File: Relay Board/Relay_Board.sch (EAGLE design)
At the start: 45 parts, among them J1 22-05-7048-04, J2 22-05-7028-02, J3 22-05-7028-02, K1 G6K-2G-Y, K2 G6K-2G-Y, K3 G6K-2G-Y, K4 G6K-2G-Y, T1 EXMACHINA-LOGO-NAME, U10 SN74LVC2G17DBVR, U9 SN74LVC2G17DBVR, X1 MSTBA2, X12 22-05-7028-02, X13 22-05-7028-02, X14 22-05-7038-03, X15 22-05-7038-03

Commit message: Add free-wheel diode on the schematic and re-route the board
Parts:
- added D1, D2, D3, D4: STPS3L40UF, diode:STPS3L40UF
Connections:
- net GND: now also D1.A, D2.A, D3.A, D4.A
- net N$24: now also D1.C
- net N$28: now also D3.C
- net N$33: now also D4.C
- net N$55: now also D2.C
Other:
- moved on the sheet: C129, C130, C131, C132, C133, C134, J2-1, J2-2, J3-1, J3-2, K1, K2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

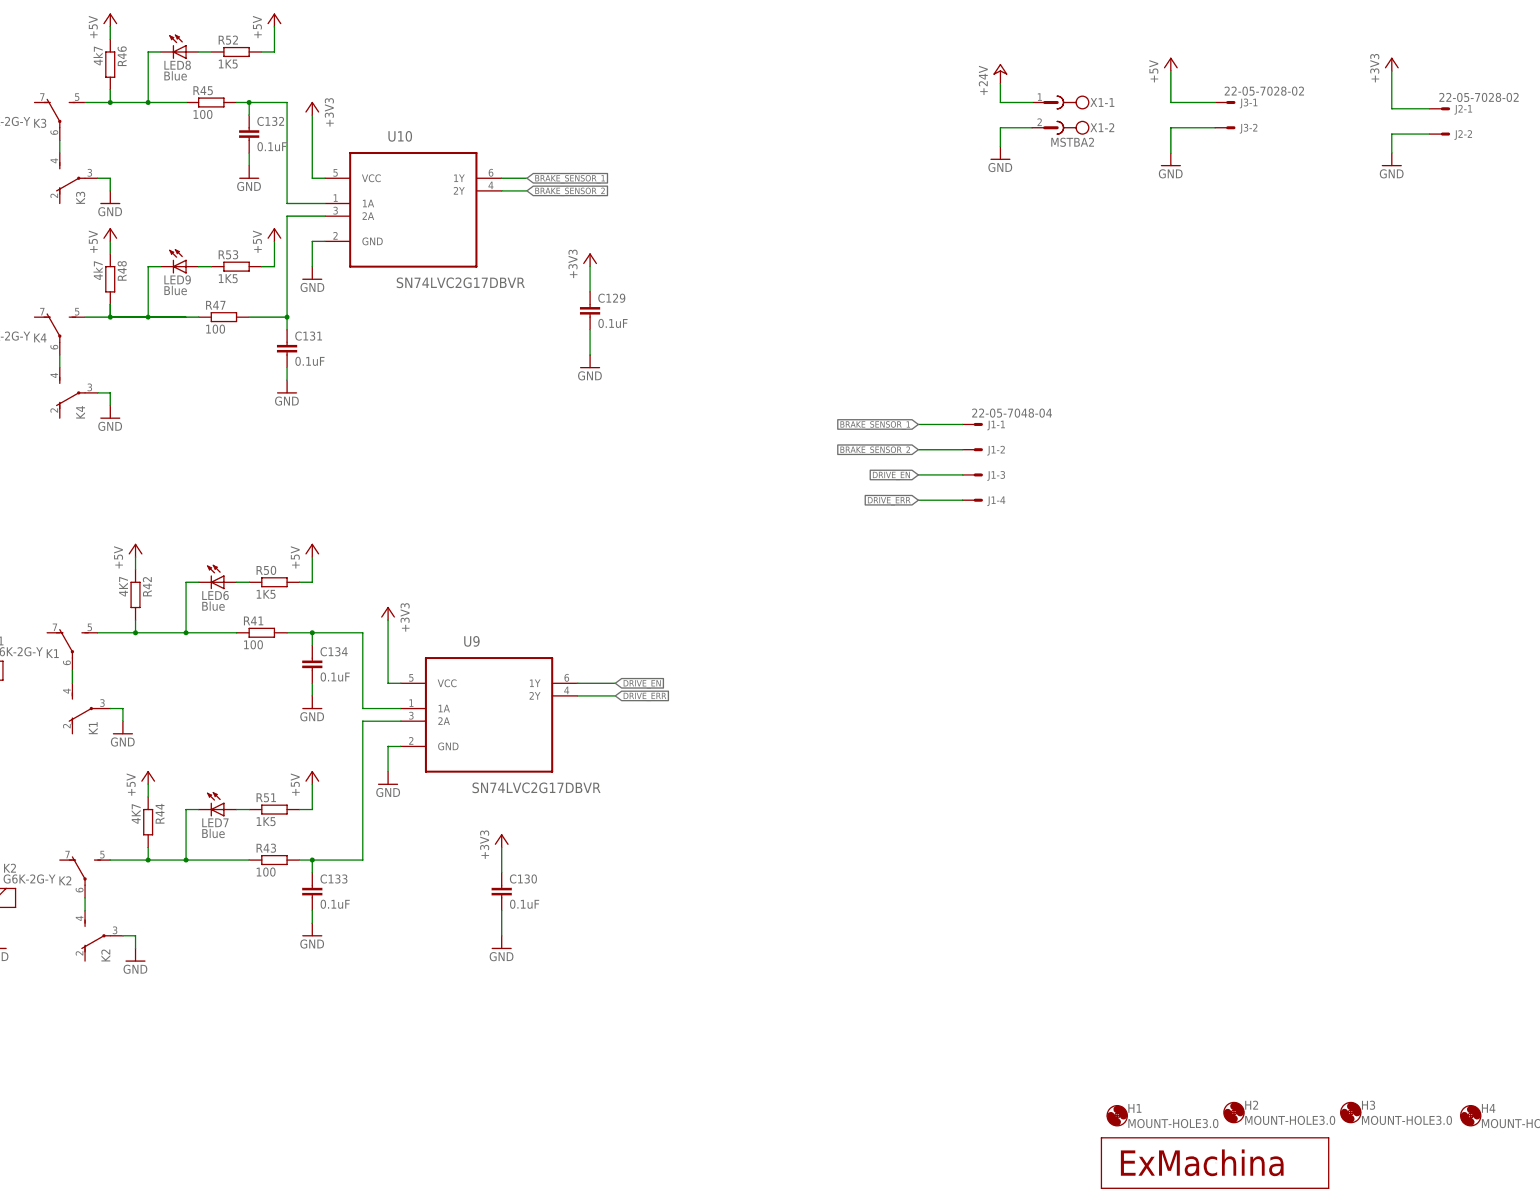
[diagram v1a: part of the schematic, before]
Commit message: Add fiducial to the board
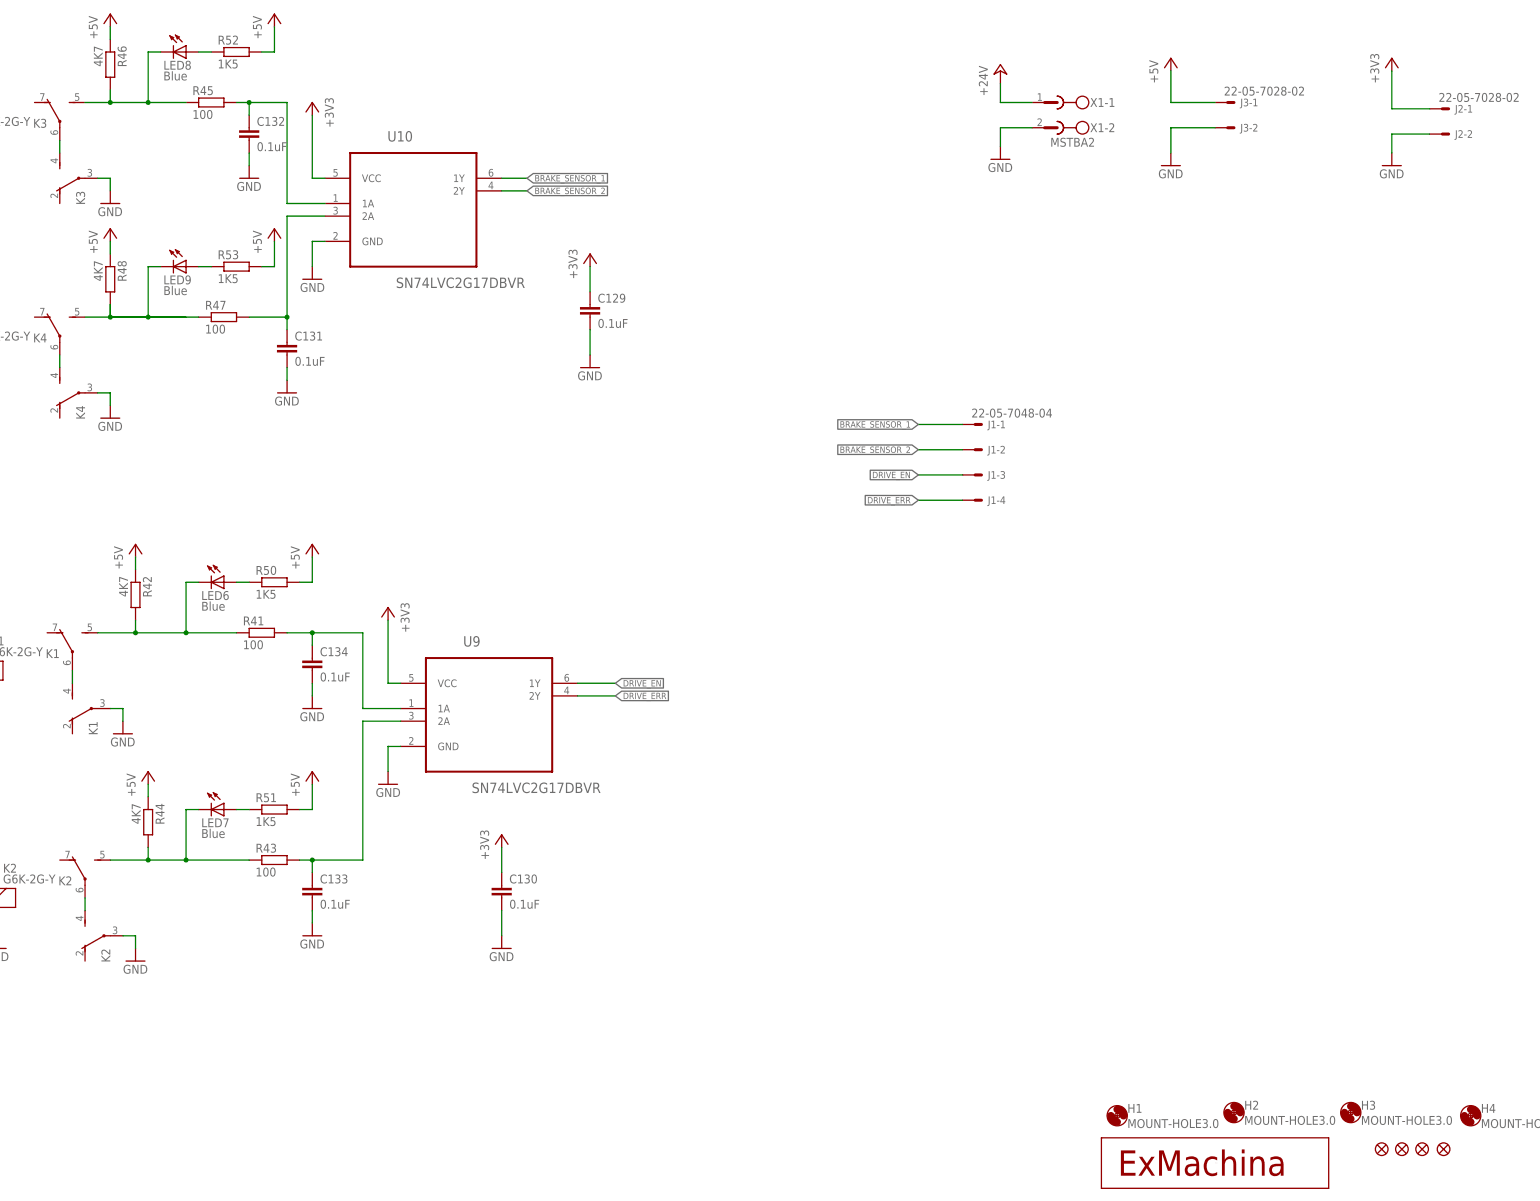
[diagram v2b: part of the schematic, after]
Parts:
- added JP1, JP2, JP3, JP4: FIDUCIAL1X2, SparkFun:FIDUCIAL1X2
- C129, C130, C131, C132, C133, C134: MPN (none) -> MC0603B104K250CT; OC_NEWARK (none) -> 06R4925
- D1, D2, D3, D4: OC_NEWARK (none) -> 06X0873
- H1, H2, H3, H4, T1: OC_NEWARK (none) -> unknown
- J1: MPN (none) -> 22-05-7048; OC_NEWARK (none) -> 26M6363
- J2, J3, X12, X13: MPN (none) -> 22-05-7028; OC_NEWARK (none) -> 25M1728
- K1, K2, K3, K4: MPN (none) -> G6K-2G-Y 24DC; OC_NEWARK (none) -> 82T9378
- LED6, LED7, LED8, LED9: MPN (none) -> OVS-0603; OC_NEWARK (none) -> 15R2205
- R108, R109, R110, R111, R41, R43, R45, R47: MPN (none) -> MCMR06X1000FTL; OC_NEWARK (none) -> 86T3504
- R42, R44: MPN (none) -> MCMR06X4701FTL; OC_NEWARK (none) -> 86T3649
- R46, R48: value 4k7 -> 4K7; MPN (none) -> MCMR06X4701FTL; OC_NEWARK (none) -> 86T3649
- R50, R51, R52, R53: MPN (none) -> MCMR06X1501FTL; OC_NEWARK (none) -> 86T3542
- U10, U9: MF (none) -> TEXAS INSTRUMENTS
- X14, X15: MPN (none) -> 22-05-7038; OC_NEWARK (none) -> 26M6362

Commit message: Change name and value size on the board
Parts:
- removed X12: 22-05-7028-02, con-molex:22-05-7028-02
- removed X14, X15: 22-05-7038-03, con-molex:22-05-7038-03
- added J5: 22-05-7048-04, con-molex:22-05-7048-04
- added J6, J7: 22-05-7028-02, con-molex:22-05-7028-02
- J1: value 22-05-7048-04 -> 22-05-7038-03; device con-molex:22-05-7048-04 -> con-molex:22-05-7038-03; MPN 22-05-7048 -> 22-05-7038; OC_NEWARK 26M6363 -> 26M6362
- J2: value 22-05-7028-02 -> 22-05-7038-03; device con-molex:22-05-7028-02 -> con-molex:22-05-7038-03; MPN 22-05-7028 -> 22-05-7038; OC_NEWARK 25M1728 -> 26M6362
- JP1, JP2, JP3, JP4: OC_NEWARK (none) -> unknown
- renumbered C129 to C6, C130 to C5, C131 to C2, C132 to C1, C133 to C4, C134 to C3, LED6 to LED3, LED7 to LED4, LED8 to LED1, LED9 to LED2, R108 to R2, R109 to R1, R110 to R4, R111 to R3, R41 to R13, R42 to R7, R43 to R16, R44 to R8, R45 to R9, R46 to R5, R47 to R10, R48 to R6, R50 to R14, R51 to R15, R52 to R11, R53 to R12, U10 to U1, U9 to U2, X13 to J4
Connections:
- net +24V: now also J1-1.S, J2-1.S, J3-1.S; no longer X12-1.S, X14-1.S, X15-1.S
- net +3V3: now also J7-1.S; no longer J2-1.S
- net +5V: now also J6-1.S; no longer J3-1.S
- net BRAKE_SENSOR_1: now also J5-1.S; no longer J1-1.S
- net BRAKE_SENSOR_2: now also J5-2.S; no longer J1-2.S
- net DRIVE_EN: now also J5-3.S; no longer J1-3.S
- net DRIVE_ERR: now also J5-4.S; no longer J1-4.S
- net GND: now also J1-3.S, J2-3.S, J6-2.S, J7-2.S; no longer J2-2.S, J3-2.S, X14-3.S, X15-3.S
- net N$21: now also J1-2.S; no longer X14-2.S
- net N$23: now also J2-2.S; no longer X15-2.S
- net N$24: now also K11.+; no longer K31.+
- net N$28: now also K31.+; no longer K11.+
- net N$32: now also J3-2.S; no longer X12-2.S
- net N$33: now also K41.+; no longer K21.+
- net N$55: now also K21.+; no longer K41.+
- net N$58: now also K13.S; no longer K33.S
- net N$71: now also K23.S; no longer K43.S
- net N$73: now also K33.S; no longer K13.S
- net N$75: now also K43.S; no longer K23.S
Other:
- moved on the sheet: J1-1, J1-2, J1-3, J2-1, J2-2, J3-1, J3-2, K1, K2, K3, K4
